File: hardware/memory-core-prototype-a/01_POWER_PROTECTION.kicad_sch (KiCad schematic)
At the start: 1 part, among them J901 SHEET_INTERFACE_NOT_FITTED

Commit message: Capture ERC-validated power protection sheet
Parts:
- removed J901: SHEET_INTERFACE_NOT_FITTED, symbol Connector_Generic:Conn_01x06
- added C1, C3: 47µF 25V, Capacitor_SMD:C_1210_3225Metric, symbol Device:C_Polarized
- added C10, C6, C7, C9: 22µF 10V X7R, Capacitor_SMD:C_1206_3216Metric, symbol Device:C
- added C11: 2.2µF 10V X7R, Capacitor_SMD:C_0805_2012Metric, symbol Device:C
- added C12: 4.7µF 10V X7R, Capacitor_SMD:C_0805_2012Metric, symbol Device:C
- added C13, C14: 100nF, Capacitor_SMD:C_0805_2012Metric, symbol Device:C
- added C2, C4: 100nF 50V, Capacitor_SMD:C_0805_2012Metric, symbol Device:C
- added C5, C8: 10µF 25V X7R, Capacitor_SMD:C_1206_3216Metric, symbol Device:C
- added D1, D2: SS34 — provisional, symbol Device:D_Schottky
- added F1: 750mA hold — provisional, symbol Device:Polyfuse
- added F2: 250mA hold — provisional, symbol Device:Polyfuse
- added FB1: ≥1A low-DCR, symbol Device:L_Ferrite
- added FB2: ≥0.5A low-DCR, symbol Device:L_Ferrite
- added J1: PROTECTED ±12 V INPUT, symbol Connector_Generic:Conn_01x03
- added L1: 2.2µH; Isat ≥1.3A, symbol Device:L
- added L2: 3.3µH; Isat ≥1.3A, symbol Device:L
- added R1: 374k 1%, Resistor_SMD:R_0805_2012Metric, symbol Device:R
- added R10: 10k fault pull-up, Resistor_SMD:R_0805_2012Metric, symbol Device:R
- added R2, R4: 120k 1%, Resistor_SMD:R_0805_2012Metric, symbol Device:R
- added R3: 698k 1%, Resistor_SMD:R_0805_2012Metric, symbol Device:R
- added R5: 50k 1% — 300ms nominal, Resistor_SMD:R_0805_2012Metric, symbol Device:R
- added R6: 10k, Resistor_SMD:R_0805_2012Metric, symbol Device:R
- added R7: 10k — CWD, Resistor_SMD:R_0805_2012Metric, symbol Device:R
- added R8: 100k — EN high, Resistor_SMD:R_0805_2012Metric, symbol Device:R
- added R9: 10k — SET1 high, Resistor_SMD:R_0805_2012Metric, symbol Device:R
- added SW1: RESET / CLEAR, symbol Switch:SW_Push
- added TP1: P12_PROTECTED, symbol Connector:TestPoint
- added TP2: N12_PROTECTED, symbol Connector:TestPoint
- added TP3: DIGITAL_3V3, symbol Connector:TestPoint
- added TP4: PRE_5V453, symbol Connector:TestPoint
- added TP5: QUIET_5V, symbol Connector:TestPoint
- added TP6: FAULT_N, symbol Connector:TestPoint
- added TP7: WDI, symbol Connector:TestPoint
- added TP8: WDO_N, symbol Connector:TestPoint
- added U1: TPS62160 — 3.3V, symbol MerrinLab_PrototypeA:TPS62160DGK
- added U2: TPS62160 — 5.453V PRE, symbol MerrinLab_PrototypeA:TPS62160DGK
- added U3: TPS7A2050 — QUIET 5V, symbol MerrinLab_PrototypeA:TPS7A2050PDBV
- added U4: TPS3808G33, symbol MerrinLab_PrototypeA:TPS3808G33DBV
- added U5: TPS3431 — 200ms watchdog, symbol MerrinLab_PrototypeA:TPS3431DRB
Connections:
- net HARDWARE_FAULT_N: now also R10.2, TP6.1, TP8.1, U1.8 (PG), U2.8 (PG), U4.1 (RESET_N), U5.7 (WDO_N)
- net RAIL_3V3: now also C13.1, C14.1, C6.1, C7.1, L1.2, R1.1, R10.1, R5.1, R6.1, R7.1, R8.1, R9.1, TP3.1, U1.6 (VOS), U4.5 (SENSE), U4.6 (VDD), U5.1 (VDD)
- net RAIL_5V_CODEC: now also C12.1, TP5.1, U3.5 (OUT)
- net RAIL_N12: now also C3.2, C4.1, FB2.2, TP2.1
- net RAIL_P12: now also C1.1, C2.1, C5.1, C8.1, FB1.2, TP1.1, U1.2 (VIN), U1.3 (EN), U2.2 (VIN), U2.3 (EN)
- net WATCHDOG_HEARTBEAT: now also TP7.1, U5.6 (WDI)
- new net BUCK3V3_FB: R1.2, R2.1, U1.5 (FB)
- new net BUCK3V3_SW: L1.1, U1.7 (SW)
- new net BUCK5V45_FB: R3.2, R4.1, U2.5 (FB)
- new net BUCK5V45_SW: L2.1, U2.7 (SW)
- new net GND: C1.2, C10.2, C11.2, C12.2, C13.2, C14.2, C2.2, C3.1, C4.2, C5.2, C6.2, C7.2, C8.2, C9.2, J1.2 (Pin_2), R2.2, R4.2, SW1.2, U1.1 (PGND), U1.4 (AGND), U2.1 (PGND), U2.4 (AGND), U3.2 (GND), U4.2 (GND), U5.4 (GND), U5.9 (EP)
- new net MANUAL_RESET_N: R6.2, SW1.1, U4.3 (MR_N)
- new net N12_FUSED: D2.1 (K), F2.2
- new net N12_PROTECTED_DIODE: D2.2 (A), FB2.1
- new net P12_FUSED: D1.2 (A), F1.2
- new net P12_PROTECTED_DIODE: D1.1 (K), FB1.1
- new net RAIL_5V45_PRE: C10.1, C11.1, C9.1, L2.2, R3.1, TP4.1, U2.6 (VOS), U3.1 (IN), U3.3 (EN)
- new net RAW_N12: F2.1, J1.3 (Pin_3)
- new net RAW_P12: F1.1, J1.1 (Pin_1)
- new net SUPERVISOR_CT: R5.2, U4.4 (CT)
- new net WATCHDOG_CWD: R7.2, U5.2 (CWD)
- new net WATCHDOG_EN: R8.2, U5.3 (EN)
- new net WATCHDOG_SET1: R9.2, U5.5 (SET1)
- no-connect marks 0 -> 2
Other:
- note added: "Active-device footprints intentionally blank pending independent footprint review."
- note added: "FAULT_N wired-AND sources: U1 PG, U2 PG, U4 RESET_N, U5 WDO_N. Fault release requires all sources high; no firmware path can force a held-low net high."
- note added: "PROTECTED ±12 V • 3.3 V DIGITAL • 5.453 V PRE-RAIL • QUIET 5 V • HARDWARE FAULT"
- note added: "PWR_FLAG markers identify rails after passive protection/conversion boundaries for ERC. RAIL_5V_CODEC is driven directly by U3 and needs no source annotation."
- note added: "Provisional power-entry fuses, Schottky diodes, ferrite beads and connector remain subject to exact part selection. The topology is captured; footprints and physical power format remain blocked."
- note removed: "HIERARCHY / INTERFACE CAPTURE ONLY — CIRCUIT CONTENT NOT YET ACCEPTED"
- title: Memory Core Prototype A — POWER / PROTECTION -> Memory Core Prototype A — Power / Protection

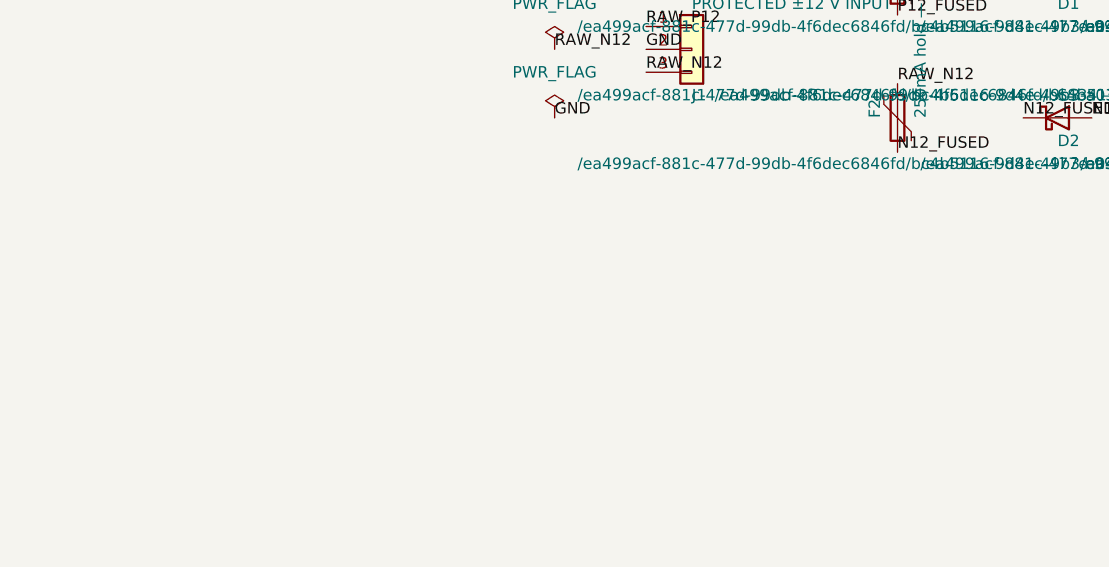
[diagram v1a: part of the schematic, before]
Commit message: Capture ERC-validated controls and state sheet
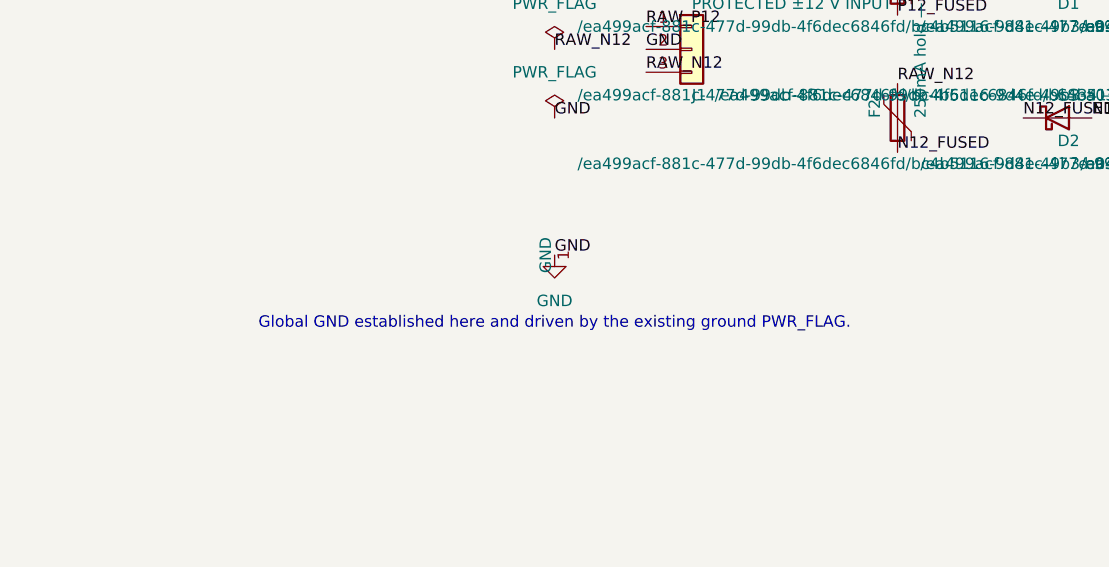
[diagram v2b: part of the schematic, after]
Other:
- note added: "Global GND established here and driven by the existing ground PWR_FLAG."
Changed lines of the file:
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@@
+		)
+	)
+	(symbol
+		(lib_id "power:GND")
+		(at 20.32 114.3 0)
+		(unit 1)
+		(exclude_from_sim no)
+		(in_bom no)
+		(on_board no)
+		(dnp no)
+		(fields_autoplaced no)
+		(property "Reference" "#PWR0101"
+			(at 20.32 107.95 0.0000)
+			(effects
+				(font
+					(size 1.27 1.27)
+				)
+				(justify left)
+				(hide yes)
+			)
+		)
+		(property "Value" "GND"
+			(at 20.32 119.38 0)
+			(effects
+				(font
+					(size 1.27 1.27)
+				)
+			)
+		)
+		(pin "1"
+		)
+		(instances
+			(project "simple_circuit"
+				(path "/c0b2e286-e7b9-4fc3-88a6-7a0b54ccc874"
+					(reference "#PWR0101")
+					(unit 1)
+				)
+			)
 		)
 	)
@@
 	)
 	(label "RAIL_P12"
-		(at 137.16 76.2 0)
+		(at 137.16 76.2 0.0000)
 		(effects
 			(font
@@
 	)
 	(label "RAIL_N12"
-		(at 137.16 106.68 0)
-		(effects
-			(font
-				(size 1.27 1.27)
-			)
-			(justify left bottom)
-		)
-	)
-	(label "RAIL_3V3"
-		(at 248.92 66.04 0)
+		(at 137.16 106.68 0.0000)
+		(effects
+			(font
+				(size 1.27 1.27)
+			)
+			(justify left bottom)
+		)
+	)
+	(label "RAIL_3V3"
+		(at 248.92 66.04 0.0000)
 		(effects
 			(font
@@
 	)
 	(label "RAIL_5V45_PRE"
-		(at 248.92 116.84 0)
+		(at 248.92 116.84 0.0000)
+		(effects
+			(font
+				(size 1.27 1.27)
+			)
+			(justify left bottom)
+		)
+	)
+	(label "GND"
+		(at 20.32 114.3 0)
 		(effects
 			(font
@@
 		(effects
 			(font
+				(size 1.27 1.27)
+			)
+		)
+	)
+	(text "Global GND established here and driven by the existing ground PWR_FLAG."
+		(exclude_from_sim no)
+		(at 20.32 121.92 0.0000)
+		(effects
+			(font

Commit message: Complete final integrated schematic review
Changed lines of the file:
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@@
 	)
 	(hierarchical_label "RAIL_P12"
-		(shape input)
+		(shape output)
 		(at 391.16 43.18 0.0000)
 		(effects
@@
 	)
 	(hierarchical_label "RAIL_N12"
-		(shape input)
+		(shape output)
 		(at 391.16 50.8 0.0000)
 		(effects
@@
 	)
 	(hierarchical_label "RAIL_3V3"
-		(shape input)
+		(shape output)
 		(at 391.16 58.42 0.0000)
 		(effects
@@
 	)
 	(hierarchical_label "RAIL_5V_CODEC"
-		(shape input)
+		(shape output)
 		(at 391.16 66.04 0.0000)
 		(effects
@@
 	)
 	(hierarchical_label "HARDWARE_FAULT_N"
-		(shape input)
+		(shape output)
 		(at 391.16 73.66 0.0000)
 		(effects
